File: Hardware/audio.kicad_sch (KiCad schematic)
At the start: 35 parts, among them J13 ANT_BNC, J14 ANT_BNC, J15 Audio IN, Q3 MMBT2222A, U10 Si4732, U9 LM358, X1 Q13FC1350000400

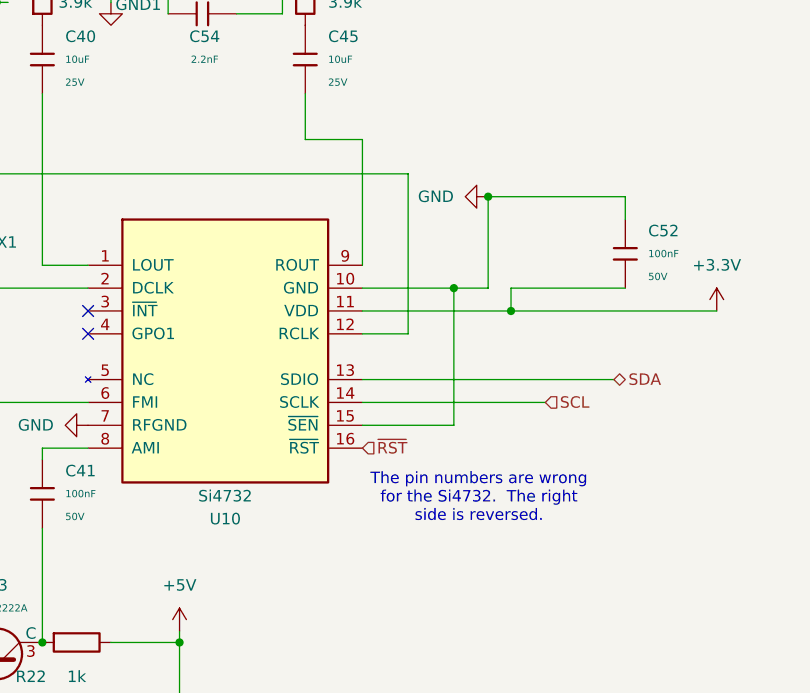
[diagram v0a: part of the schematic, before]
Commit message: Actual pcb and sch changes
I switched the pin numbers that were backwards
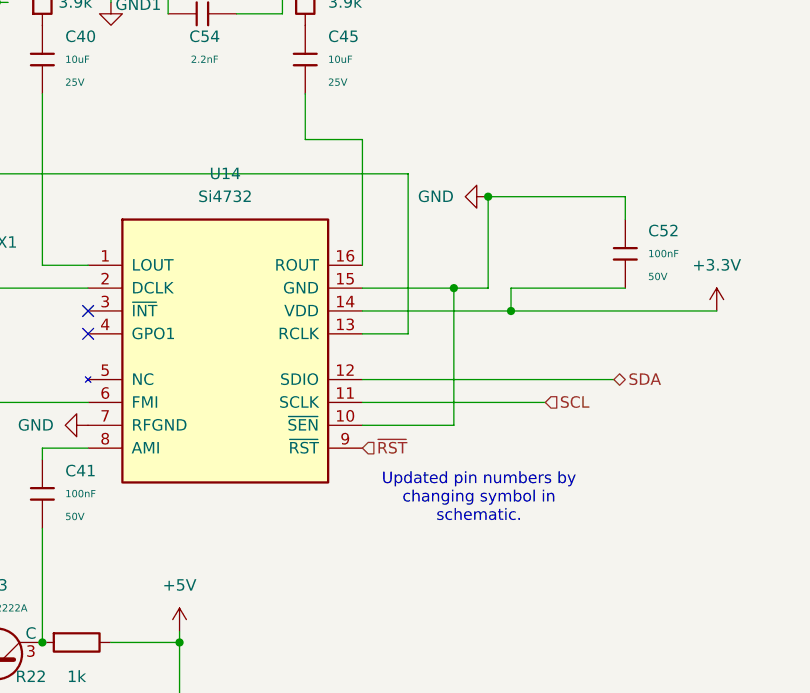
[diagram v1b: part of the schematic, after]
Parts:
- removed U10: Si4732, Package_SO:SOIC-16_3.9x9.9mm_P1.27mm, symbol RF_AM_FM:Si4735-D60-GU
- added U14: Si4732, Package_SO:SOIC-16_3.9x9.9mm_P1.27mm, symbol RF_AM_FM:Si4735-D60-GU
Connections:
- net +3.3V: now also U14.14 (VDD)
- net GND: now also U14.10 (~{SEN}), U14.15 (GND), U14.7 (RFGND)
- net SCL: now also U14.11 (SCLK)
- net SDA: now also U14.12 (SDIO)
- net ~{RST}: now also U14.9 (~{RST})
- net at C36.2, X1.2: now also U14.13 (RCLK)
- net at C41.1: now also U14.8 (AMI)
- net at C37.1, X1.1: now also U14.2 (DCLK)
- net at C45.2: now also U14.16 (ROUT)
- net at C40.2: now also U14.1 (LOUT)
- net at C34.2: now also U14.6 (FMI)
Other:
- note added: "Updated pin numbers by changing symbol in schematic."
- note removed: "The pin numbers are wrong for the Si4732. The right side is reversed."
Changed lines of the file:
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@@
 	(generator_version "9.0")
 	(paper "A4")
-	(text "The pin numbers are wrong\nfor the Si4732.  The right\nside is reversed."
+	(text "Updated pin numbers by \nchanging symbol in \nschematic."
 		(exclude_from_sim no)
 		(at 119.634 133.858 0)
@@
 	)
 	(symbol
+		(lib_id "RF_AM_FM:Si4735-D60-GU")
+		(at 91.44 115.57 0)
+		(unit 1)
+		(exclude_from_sim no)
+		(in_bom yes)
+		(on_board yes)
+		(dnp no)
+		(fields_autoplaced yes)
+		(property "Reference" "U14"
+			(at 91.44 97.79 0)
+			(effects
+				(font
+					(size 1.27 1.27)
+				)
+			)
+		)
+		(property "Value" "Si4732"
+			(at 91.44 100.33 0)
+			(effects
+				(font
+					(size 1.27 1.27)
+				)
+			)
+		)
+		(property "Footprint" "Package_SO:SOIC-16_3.9x9.9mm_P1.27mm"
+			(at 97.79 133.35 0)
+			(do_not_autoplace yes)
+			(effects
+				(font
+					(size 1.27 1.27)
+				)
+				(justify left)
+				(hide yes)
+			)
+		)
+		(property "Datasheet" "https://wmsc.lcsc.com/wmsc/upload/file/pdf/v2/lcsc/2202032030_SKYWORKS-SILICON-LABS-SI4732-A10-GSR_C2155558.pdf"
+			(at 92.71 140.97 0)
+			(do_not_autoplace yes)
+			(effects
+				(font
+					(size 1.27 1.27)
+				)
+				(hide yes)
+			)
+		)
+		(property "Description" "AM/FM/SW/LW Broadcast Radio Receiver with RDS/RBDS"
+			(at 79.756 157.734 0)
+			(effects
+				(font
+					(size 1.27 1.27)
+				)
+				(hide yes)
+			)
+		)
+		(property "LCSC" "C2155558"
+			(at 91.44 115.57 0)
+			(effects
+				(font
+					(size 1.27 1.27)
+				)
+				(hide yes)
+			)
+		)
+		(property "JLCPCB #" ""
+			(at 91.44 115.57 0)
+			(effects
+				(font
+					(size 1.27 1.27)
+				)
+				(hide yes)
+			)
+		)
+		(pin "9"
+		)
+		(pin "10"
+		)
+		(pin "11"
+		)
+		(pin "12"
+		)
+		(pin "13"
+		)
+		(pin "8"
+		)
+		(pin "16"
+		)
+		(pin "15"
+		)
+		(pin "14"
+		)
+		(pin "2"
+		)
+		(pin "1"
+		)
+		(pin "3"
+		)
+		(pin "4"
+		)
+		(pin "5"
+		)
+		(pin "6"
+		)
+		(pin "7"
+		)
+		(instances
+			(project ""
+				(path "/4d45bd57-073c-4b61-a56d-da596d50cf10/7c7cf773-d00e-4ff4-9968-8b6516778136"
+					(reference "U14")
+					(unit 1)
+				)
+			)
+		)
+	)
+	(symbol
 		(lib_id "Amplifier_Operational:LM358")
 		(at 139.7 62.23 0)
@@
 					(unit 1)
 				)
-			)
-		)
-	)
-	(symbol
-		(lib_name "Si4735-D60-GU_1")
-		(lib_id "RF_AM_FM:Si4735-D60-GU")
-		(at 91.44 115.57 0)
-		(unit 1)
-		(exclude_from_sim no)
-		(in_bom yes)
-		(on_board yes)
-		(dnp no)
-		(property "Reference" "U10"
-			(at 91.44 136.144 0)
-			(effects
-				(font
-					(size 1.27 1.27)
-				)
-			)
-		)
-		(property "Value" "Si4732"
-			(at 91.44 133.604 0)
-			(effects
-				(font
-					(size 1.27 1.27)
-				)
-			)
-		)
-		(property "Footprint" "Package_SO:SOIC-16_3.9x9.9mm_P1.27mm"
-			(at 97.79 133.35 0)
-			(do_not_autoplace yes)
-			(effects
-				(font
-					(size 1.27 1.27)
-				)
-				(justify left)
-				(hide yes)
-			)
-		)
-		(property "Datasheet" "https://wmsc.lcsc.com/wmsc/upload/file/pdf/v2/lcsc/2202032030_SKYWORKS-SILICON-LABS-SI4732-A10-GSR_C2155558.pdf"
-			(at 92.71 140.97 0)
-			(do_not_autoplace yes)
-			(effects
-				(font
-					(size 1.27 1.27)
-				)
-				(hide yes)
-			)
-		)
-		(property "Description" "AM/FM/SW/LW Broadcast Radio Receiver with RDS/RBDS"
-			(at 79.756 157.734 0)
-			(effects
-				(font
-					(size 1.27 1.27)
-				)
-				(hide yes)
-			)
-		)
-		(property "LCSC" "C2155558"
-			(at 91.44 115.57 0)
-			(effects
-				(font
-					(size 1.27 1.27)
-				)
-				(hide yes)
-			)
-		)
-		(property "JLCPCB #" ""
-			(at 91.44 115.57 0)
-			(effects
-				(font
-					(size 1.27 1.27)
-				)
-				(hide yes)
-			)
-		)
-		(pin "13"
-		)
-		(pin "15"
-		)
-		(pin "12"
-		)
-		(pin "5"
-		)
-		(pin "6"
-		)
-		(pin "7"
-		)
-		(pin "1"
-		)
-		(pin "2"
-		)
-		(pin "11"
-		)
-		(pin "9"
-		)
-		(pin "16"
-		)
-		(pin "3"
-		)
-		(pin "4"
-		)
-		(pin "8"
-		)
-		(pin "14"
-		)
-		(pin "10"
-		)
-		(instances
-			(project "Audio_in_usd_sound_rp_pico"
-				(path "/4d45bd57-073c-4b61-a56d-da596d50cf10/7c7cf773-d00e-4ff4-9968-8b6516778136"
-					(reference "U10")
-					(unit 1)
-				)
